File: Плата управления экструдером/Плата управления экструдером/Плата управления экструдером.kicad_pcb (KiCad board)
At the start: 2 copper layers, 42 x 42 mm, 34 parts, among them J1 USB_C_Receptacle_USB2.0_16P, Q1 IRLB8721, Q2 IRLB8721, Q3 IRLB8721, U1 ATmega328P-A, U3 CH340N, Y1 Crystal

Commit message: Плата управления раздел
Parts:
- added H1: MountingHole, MountingHole:MountingHole_3.2mm_M3, F.Cu at (165.0, 82.0)
- added H2: MountingHole, MountingHole:MountingHole_3.2mm_M3, F.Cu at (198.0, 82.0)
- added H3: MountingHole, MountingHole:MountingHole_3.2mm_M3, F.Cu at (164.0, 116.5)
- added H4: MountingHole, MountingHole:MountingHole_3.2mm_M3, F.Cu at (198.0, 116.0)
- C1, C10, C11, C2, C4, C5, C6, C7, C8, C9, R1, R2, R3, R4, R5, R6, R7: moved to B.Cu
- Y1: footprint Crystal:Crystal_HC49-U_Vertical -> Crystal:Crystal_SMD_HC49-SD_HandSoldering
- moved C1 92.3 mm to (196.1, 93.5), turned to 0 degrees
- moved C2 86.2 mm to (190.1, 92.5), turned to 0 degrees
- moved Y1 80.9 mm to (180.1, 115.5)
- moved U3 80.3 mm to (181.0, 92.5)
- moved U1 63.1 mm to (181.0, 106.5)
- moved J1 62.0 mm to (181.0, 80.5)
- moved R1 43.2 mm to (169.0, 109.5), turned to 0 degrees
- moved R2 43.2 mm to (169.0, 106.5), turned to 0 degrees
- moved R3 43.2 mm to (169.0, 103.6), turned to 0 degrees
- moved R4 43.2 mm to (169.0, 100.6), turned to 0 degrees
- moved R5 43.2 mm to (169.0, 97.7), turned to 0 degrees
- moved R6 43.2 mm to (169.0, 94.7), turned to 0 degrees
- moved R7 43.2 mm to (169.0, 91.8), turned to 0 degrees
- moved extruder1 39.0 mm to (96.6, 131.5), turned to -90 degrees
- moved cooler_mod1 35.0 mm to (138.0, 81.8)
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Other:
- board size 42 x 42 mm -> 100.2 x 42 mm

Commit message: Коннекторы
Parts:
- added J5: Conn_01x08_Pin, Connector_PinSocket_2.54mm:PinSocket_1x08_P2.54mm_Vertical, F.Cu at (197.0, 89.4)
- C1, C10, C11, C2, C4, C5, C6, C7, C8, C9, J1, R1, R2, R3, R4, R5, R6, R7, U1, U3: moved to F.Cu
- Y1: footprint Crystal:Crystal_SMD_HC49-SD_HandSoldering -> Crystal:Crystal_HC49-4H_Vertical; moved to F.Cu
- moved A1 21.8 mm to (108.7, 100.7), turned to 0 degrees
- moved extruder1 19.0 mm to (101.0, 113.0), turned to 90 degrees
- moved C1 6.80 mm to (189.9, 96.5), turned to 180 degrees
- moved R1 5.48 mm to (163.5, 109.5), turned to 180 degrees
- moved R2 5.48 mm to (163.5, 106.5), turned to 180 degrees
- moved R3 5.48 mm to (163.5, 103.6), turned to 180 degrees
- moved R4 5.48 mm to (163.5, 100.6), turned to 180 degrees
- moved R5 5.48 mm to (163.5, 97.7), turned to 180 degrees
- moved R6 5.48 mm to (163.5, 94.7), turned to 180 degrees
- moved R7 5.48 mm to (163.5, 91.8), turned to 180 degrees
- moved C10 4.08 mm to (168.3, 91.4), turned to 180 degrees
- moved C11 4.08 mm to (168.3, 88.4), turned to 180 degrees
- moved C4 4.08 mm to (168.3, 109.5), turned to 180 degrees
- moved C5 4.08 mm to (168.3, 106.5), turned to 180 degrees
- moved C6 4.08 mm to (168.3, 103.4), turned to 180 degrees
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
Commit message: Правка платы
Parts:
- removed cooler_mod2: Conn_01x02_Pin, Connector_JST:JST_XH_B2B-XH-A_1x02_P2.50mm_Vertical
- added J6: Conn_01x08_Pin, Connector_PinSocket_2.54mm:PinSocket_1x08_P2.54mm_Vertical, F.Cu at (200.0, 89.7)
- added J7: Conn_01x08_Pin, Connector_PinHeader_2.54mm:PinHeader_1x08_P2.54mm_Vertical, B.Cu at (103.8, 89.7)
- added J8: Conn_01x08_Pin, Connector_PinHeader_2.54mm:PinHeader_1x08_P2.54mm_Vertical, B.Cu at (141.8, 89.7)
- added J9: Conn_02x03_Odd_Even, Connector_PinHeader_2.54mm:PinHeader_2x03_P2.54mm_Vertical, F.Cu at (118.7, 90.7)
- added bl_touch1: Conn_01x05_Pin, Connector_JST:JST_XH_B5B-XH-A_1x05_P2.50mm_Vertical, F.Cu at (129.5, 79.9)
- moved R7 92.7 mm to (77.8, 127.0)
- moved switch1 74.5 mm to (107.1, 116.8)
- moved C11 71.3 mm to (97.0, 87.0)
- moved R1 70.1 mm to (147.2, 41.3)
- moved C7 57.7 mm to (119.6, 131.4)
- moved R6 53.0 mm to (147.2, 44.3)
- moved C6 51.9 mm to (124.6, 131.4)
- moved term1 50.4 mm to (141.0, 116.8)
- moved C5 48.9 mm to (124.6, 128.4)
- moved C8 47.6 mm to (148.2, 54.3)
- moved C10 47.6 mm to (148.2, 48.3)
- moved R5 45.8 mm to (129.6, 128.4)
- moved R2 37.3 mm to (139.5, 135.0)
- moved extruder1 36.4 mm to (115.9, 79.8), turned to 0 degrees
- moved cooler_mod1 35.3 mm to (132.6, 116.8)
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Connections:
- A1 pad 15: Net-(A1-STEP) -> /STEP_PB
- A1 pad 16: Net-(A1-DIR) -> /DIR_PB
- A1 pad 9: Net-(A1-~{ENABLE}) -> /ENABLE_PB
- C11 pad 1: /termistor -> /termistor_PB
- J5 pad 1: unconnected-(J5-Pin_1-Pad1) -> /STEP
- J5 pad 2: unconnected-(J5-Pin_2-Pad2) -> /DIR
- J5 pad 3: unconnected-(J5-Pin_3-Pad3) -> /ENABLE
- POWER_IN_24V1 pad 1: Net-(A1-VMOT) -> GND
- POWER_IN_24V1 pad 2: GND -> Net-(A1-VMOT)
- Q1 pad 1: /fan_control -> /fan_control_PB
- Q2 pad 1: /cooler -> /cooler_PB
- Q2 pad 2: +24V -> Net-(Q2-D)
- Q3 pad 1: /heater -> /heater_PB
- R4 pad 1: /cooler -> /cooler_PB
- R5 pad 1: /fan_control -> /fan_control_PB
- R6 pad 1: /heater -> /heater_PB
- R7 pad 2: /termistor -> /termistor_PB
- U1 pad 1: Net-(A1-DIR) -> /DIR
- U1 pad 12: /switch -> unconnected-(U1-PB0-Pad12)
- U1 pad 13: /BL_Z-min -> unconnected-(U1-PB1-Pad13)
- U1 pad 17: unconnected-(U1-PB5-Pad17) -> /switch
- U1 pad 19: unconnected-(U1-ADC6-Pad19) -> /termistor
- U1 pad 2: Net-(A1-~{ENABLE}) -> /ENABLE
- U1 pad 23: /termistor -> /BL_Z-min
- U1 pad 25: unconnected-(U1-PC2-Pad25) -> /heater
- U1 pad 26: /heater -> /fan_control
- U1 pad 27: /fan_control -> /cooler
- U1 pad 28: /cooler -> unconnected-(U1-PC5-Pad28)
- U1 pad 32: Net-(A1-STEP) -> /STEP
- cooler_mod1 pad 1: Net-(cooler_mod1-Pin_1) -> +24V
- cooler_mod1 pad 2: +24V -> Net-(Q2-D)
- switch1 pad 1: /switch -> /switch_PB
- term1 pad 1: /termistor -> /termistor_PB

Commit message: Начало трассировки
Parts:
- added J10: Conn_01x08_Pin, Connector_PinSocket_2.54mm:PinSocket_1x08_P2.54mm_Vertical, F.Cu at (172.1, 117.5)
- moved C4 64.2 mm to (148.4, 134.2)
- moved C8 63.2 mm to (190.1, 101.7)
- moved R2 60.7 mm to (177.3, 87.5)
- moved R1 52.6 mm to (172.2, 87.5), turned to 0 degrees
- moved switch1 33.8 mm to (141.0, 116.7)
- moved Y1 28.9 mm to (168.7, 108.0), turned to -45 degrees
- moved C1 17.5 mm to (172.2, 104.5), turned to 135 degrees
- moved C2 17.0 mm to (175.7, 108.4), turned to -45 degrees
- moved R6 12.2 mm to (158.9, 47.7)
- moved cooler_mod1 8.48 mm to (124.1, 116.7)
- moved fan1 8.48 mm to (107.1, 116.7)
- moved heater1 8.48 mm to (115.6, 116.7)
- moved term1 8.48 mm to (132.6, 116.7)
- moved U3 7.72 mm to (173.4, 93.8), turned to -90 degrees
- moved U1 2.28 mm to (181.7, 101.3)
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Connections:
- J5 pad 1: /STEP -> +5V
- J5 pad 2: /DIR -> unconnected-(J5-Pin_2-Pad2)
- J5 pad 3: /ENABLE -> unconnected-(J5-Pin_3-Pad3)
- J5 pad 5: unconnected-(J5-Pin_5-Pad5) -> /ENABLE
- J5 pad 6: unconnected-(J5-Pin_6-Pad6) -> /STEP
- J5 pad 7: unconnected-(J5-Pin_7-Pad7) -> /DIR
- J6 pad 1: unconnected-(J6-Pin_1-Pad1) -> /BL_Z-min
- J6 pad 2: unconnected-(J6-Pin_2-Pad2) -> /BL_contr_signal
- J6 pad 3: /cooler -> /fan_control
- J6 pad 4: /fan_control -> /heater
- J6 pad 5: /heater -> /cooler
- J6 pad 6: /BL_contr_signal -> GND
- J6 pad 7: /BL_Z-min -> /termistor
- J6 pad 8: /termistor -> /switch
- J7 pad 1: /STEP_PB -> +5V
- J7 pad 2: /ENABLE_PB -> unconnected-(J7-Pin_2-Pad2)
- J7 pad 3: /DIR_PB -> unconnected-(J7-Pin_3-Pad3)
- J7 pad 5: unconnected-(J7-Pin_5-Pad5) -> /ENABLE_PB
- J7 pad 6: unconnected-(J7-Pin_6-Pad6) -> /STEP_PB
- J7 pad 7: unconnected-(J7-Pin_7-Pad7) -> /DIR_PB
- J8 pad 6: unconnected-(J8-Pin_6-Pad6) -> GND
- J8 pad 7: unconnected-(J8-Pin_7-Pad7) -> /termistor_PB
- J8 pad 8: unconnected-(J8-Pin_8-Pad8) -> /switch_PB
- U1 pad 1: /DIR -> /STEP
- U1 pad 10: unconnected-(U1-PD6-Pad10) -> /PD6
- U1 pad 11: unconnected-(U1-PD7-Pad11) -> /PD7
- U1 pad 12: unconnected-(U1-PB0-Pad12) -> /PB0
- U1 pad 13: unconnected-(U1-PB1-Pad13) -> /PB1
- U1 pad 14: unconnected-(U1-PB2-Pad14) -> /PB2
- U1 pad 15: unconnected-(U1-PB3-Pad15) -> /PB3
- U1 pad 16: unconnected-(U1-PB4-Pad16) -> /PB4
- U1 pad 2: /ENABLE -> /DIR
- U1 pad 23: /BL_Z-min -> /cooler
- U1 pad 24: /BL_contr_signal -> /heater
- U1 pad 25: /heater -> /fan_control
- U1 pad 26: /fan_control -> /BL_contr_signal
- U1 pad 27: /cooler -> /BL_Z-min
- U1 pad 32: /STEP -> /ENABLE
- U1 pad 9: unconnected-(U1-PD5-Pad9) -> /PD5
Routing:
- net /BL_Z-min: track 0.00 -> 20.9 mm
- net /BL_contr_signal: track 0.00 -> 18.8 mm
- net /ENABLE: track 0.00 -> 18.0 mm
- net /DIR: track 0.00 -> 17.8 mm
- net /STEP: track 0.00 -> 17.1 mm
- net /fan_control: track 0.00 -> 16.5 mm
- net /switch: track 0.00 -> 15.6 mm
- net /termistor: track 0.00 -> 15.4 mm
- net /PD5: track 0.00 -> 14.9 mm
- net /heater: track 0.00 -> 14.7 mm
- net /cooler: track 0.00 -> 14.4 mm
- net /PB4: track 0.00 -> 14.3 mm
- net /PD6: track 0.00 -> 14.1 mm
- net /PB3: track 0.00 -> 13.6 mm
- net /PD7: track 0.00 -> 13.4 mm
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
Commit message: Трассировка вечером
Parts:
- moved C4 58.1 mm to (185.0, 89.0)
- moved R3 29.3 mm to (196.5, 63.0)
- moved C9 24.8 mm to (198.0, 66.0)
- moved R2 3.20 mm to (180.3, 88.5)
- moved J1 3.11 mm to (178.1, 80.4)
- moved U3 1.54 mm to (174.7, 92.9), turned to 0 degrees
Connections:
- A1 pad 8: Net-(A1-VMOT) -> +24V
- C3 pad 1: Net-(A1-VMOT) -> +24V
- POWER_IN_24V1 pad 2: Net-(A1-VMOT) -> +24V
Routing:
- net +5V: track 0.00 -> 39.4 mm
- net /DIR_PB: track 0.00 -> 23.5 mm
- net /STEP_PB: track 0.00 -> 19.9 mm
- net /termistor_PB: track 0.00 -> 15.7 mm
- net /BL_contr_signal_PB: track 0.00 -> 15.3 mm
- net Net-(A1-MS1): track 0.00 -> 12.6 mm
- net /BL_Z-min_PB: track 0.00 -> 10.7 mm
- net Net-(A1-MS2): track 0.00 -> 9.03 mm
- net Net-(A1-2B): track 0.00 -> 8.56 mm
- net Net-(A1-2A): track 0.00 -> 8.54 mm
- net Net-(A1-1A): track 0.00 -> 8.53 mm
- net Net-(A1-1B): track 0.00 -> 8.51 mm
- net Net-(A1-MS3): track 0.00 -> 5.44 mm
- net /ENABLE_PB: track 0.00 -> 3.62 mm
- added copper zone on B.Cu, net +24V

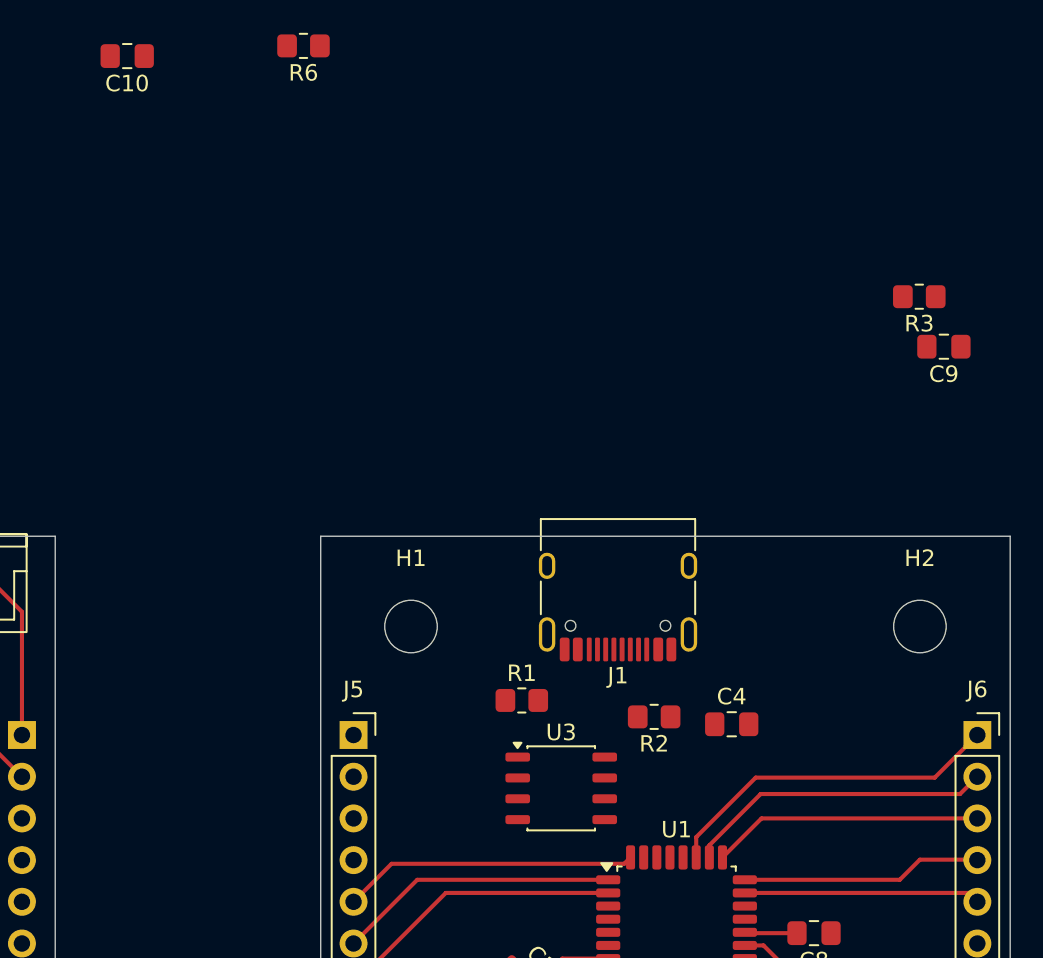
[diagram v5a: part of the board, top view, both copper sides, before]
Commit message: Трассировка USB type C
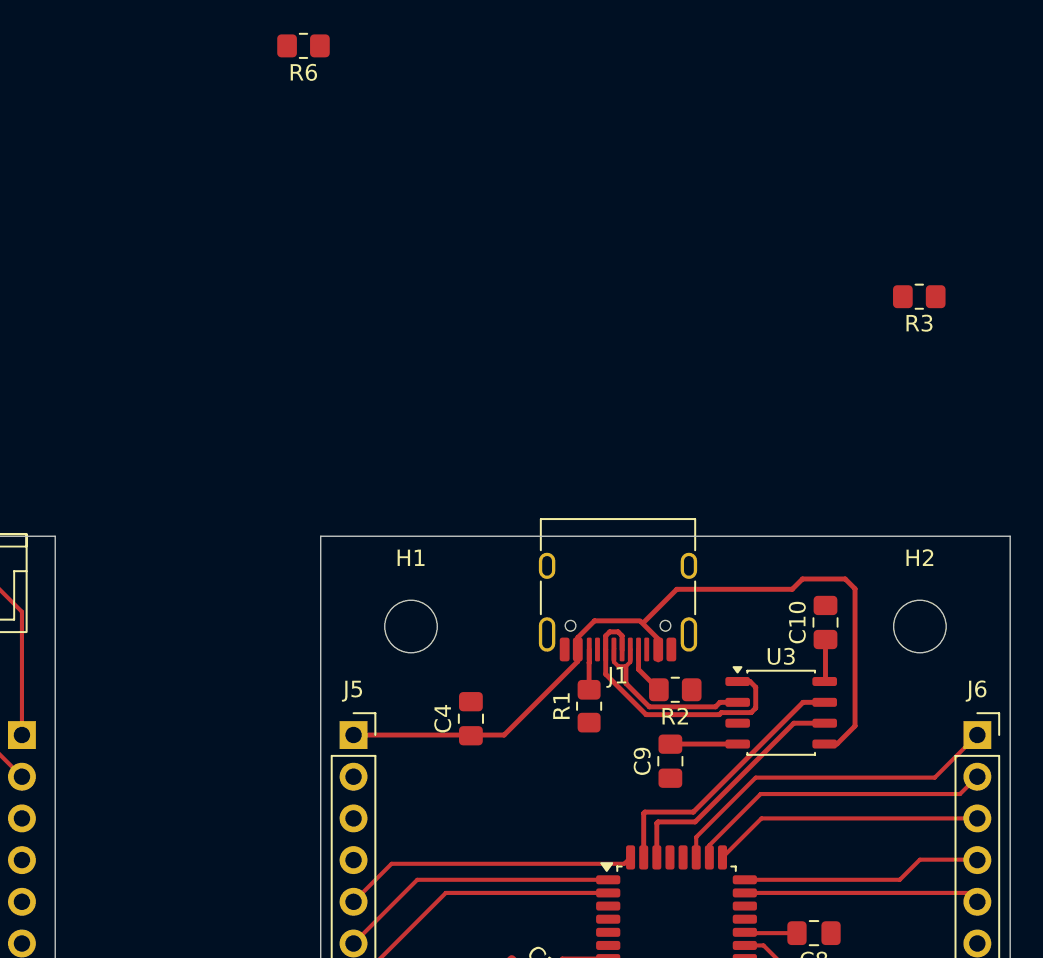
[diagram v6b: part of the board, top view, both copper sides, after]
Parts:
- moved C10 54.8 mm to (190.8, 82.8), turned to 90 degrees
- moved C9 30.3 mm to (181.3, 91.2), turned to 90 degrees
- moved C4 15.9 mm to (169.2, 88.7), turned to 90 degrees
- moved U3 14.2 mm to (188.1, 88.3)
- moved R1 4.11 mm to (176.3, 87.9), turned to 90 degrees
- moved R2 2.09 mm to (181.6, 86.9)
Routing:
- net +5V: track 39.4 -> 88.2 mm
- net Net-(U3-UD+): track 0.00 -> 17.3 mm
- net Net-(U1-PD1): track 0.00 -> 16.5 mm
- net Net-(U1-PD0): track 0.00 -> 14.8 mm
- net Net-(U3-UD-): track 0.00 -> 11.4 mm
- net Net-(U3-~{RTS}): track 0.00 -> 4.10 mm
- net Net-(J1-CC1): track 0.00 -> 2.97 mm
- net Net-(U3-V3): track 0.00 -> 2.58 mm
- net Net-(J1-CC2): track 0.00 -> 2.46 mm

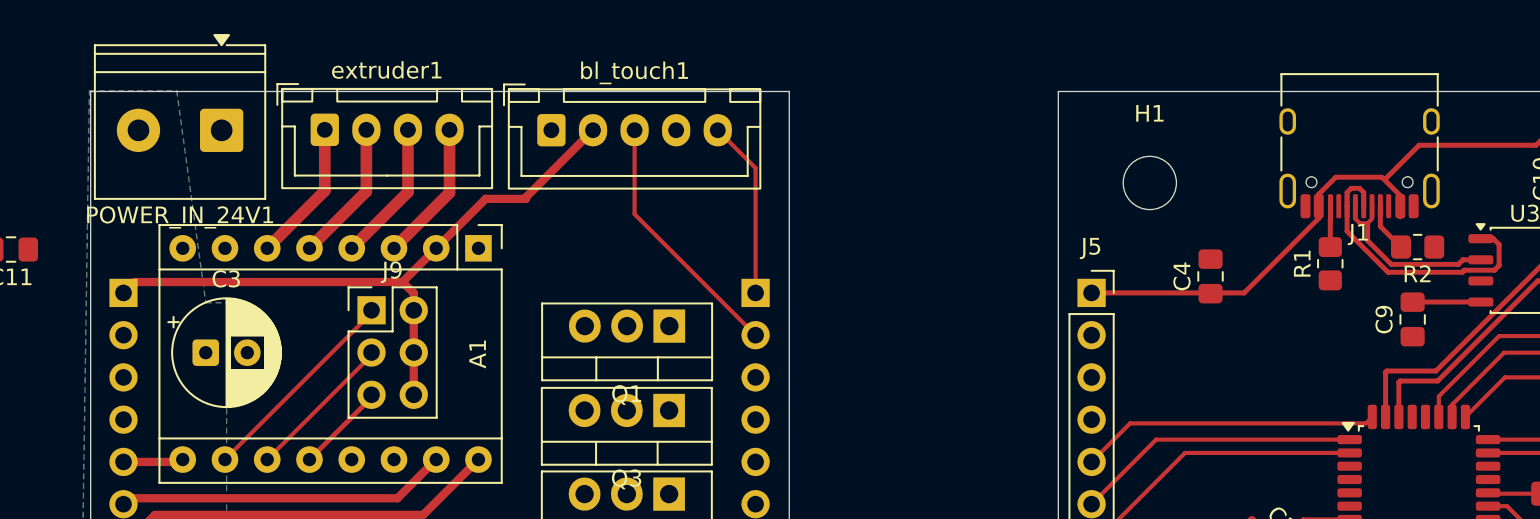
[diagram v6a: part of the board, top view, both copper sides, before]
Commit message: Изменение под PR2040-zero
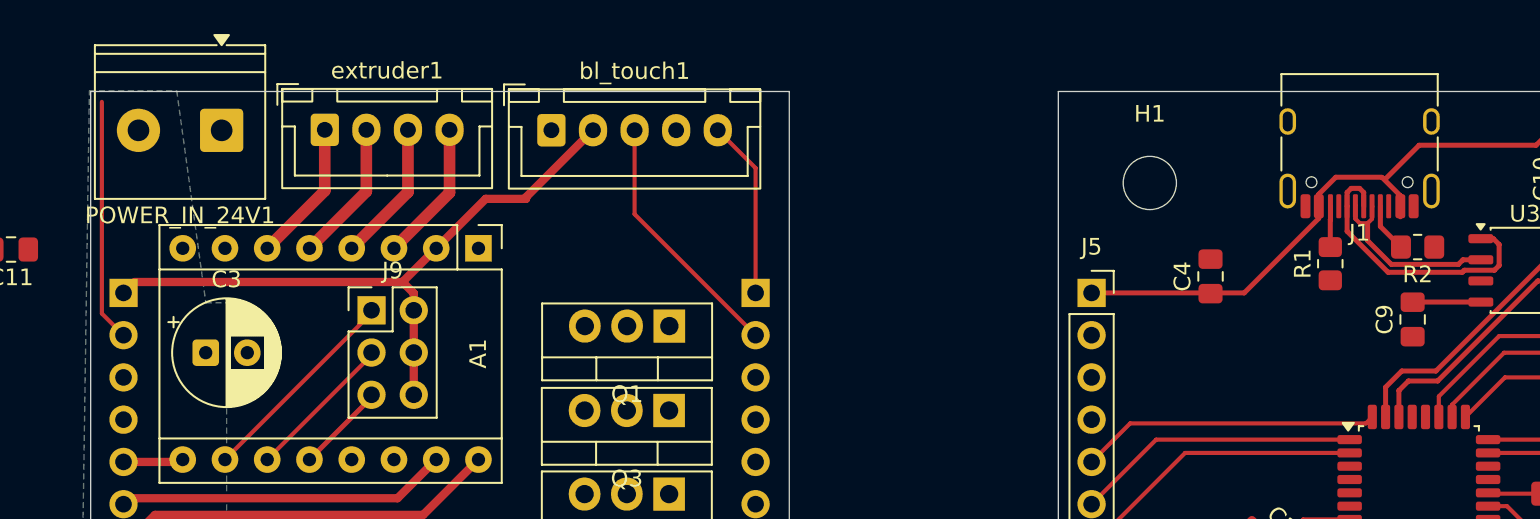
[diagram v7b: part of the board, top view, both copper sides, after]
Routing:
- net unconnected-(J7-Pin_2-Pad2): track 0.00 -> 14.6 mm
- net Net-(U1-PD1): track 16.5 -> 16.0 mm
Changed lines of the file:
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@@
 	)
 	(segment
-		(start 180.475 95.025)
-		(end 180.475 97.1125)
+		(start 190.7 88.935)
+		(end 188.822106 88.935)
+		(width 0.3)
+		(layer "F.Cu")
+		(net "Net-(U1-PD0)")
+	)
+	(segment
+		(start 182.807106 94.95)
+		(end 181.05 94.95)
 		(width 0.3)
 		(layer "F.Cu")
@@
 	)
 	(segment
-		(start 182.807106 94.95)
-		(end 180.55 94.95)
+		(start 181.05 94.95)
+		(end 180.475 95.525)
 		(width 0.3)
 		(layer "F.Cu")
@@
 	)
 	(segment
-		(start 180.55 94.95)
-		(end 180.475 95.025)
+		(start 180.475 95.525)
+		(end 180.475 97.1125)
 		(width 0.3)
 		(layer "F.Cu")
@@
 	)
 	(segment
-		(start 190.7 88.935)
-		(end 188.822106 88.935)
-		(width 0.3)
-		(layer "F.Cu")
-		(net "Net-(U1-PD0)")
-	)
-	(segment
-		(start 182.7 94.35)
-		(end 179.75 94.35)
+		(start 180.65 94.35)
+		(end 179.675 95.325)
 		(width 0.3)
 		(layer "F.Cu")
@@
 	)
 	(segment
-		(start 179.75 94.35)
-		(end 179.675 94.425)
-		(width 0.3)
-		(layer "F.Cu")
-		(net "Net-(U1-PD1)")
-	)
-	(segment
-		(start 179.675 94.425)
+		(start 179.675 95.325)
 		(end 179.675 97.1125)
 		(width 0.3)
@@
 		(start 189.385 87.665)
 		(end 182.7 94.35)
+		(width 0.3)
+		(layer "F.Cu")
+		(net "Net-(U1-PD1)")
+	)
+	(segment
+		(start 182.7 94.35)
+		(end 180.65 94.35)
 		(width 0.3)
 		(layer "F.Cu")
@@
 		(net "/DIR_PB")
 	)
+	(segment
+		(start 103.8 92.196)
+		(end 102.5 90.896)
+		(width 0.25)
+		(layer "F.Cu")
+		(net "unconnected-(J7-Pin_2-Pad2)")
+	)
+	(segment
+		(start 102.5 90.896)
+		(end 102.5 78.171)
+		(width 0.25)
+		(layer "F.Cu")
+		(net "unconnected-(J7-Pin_2-Pad2)")
+	)
 	(zone
